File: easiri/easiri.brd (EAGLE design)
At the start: 50.8 x 50.8 mm, 44 parts

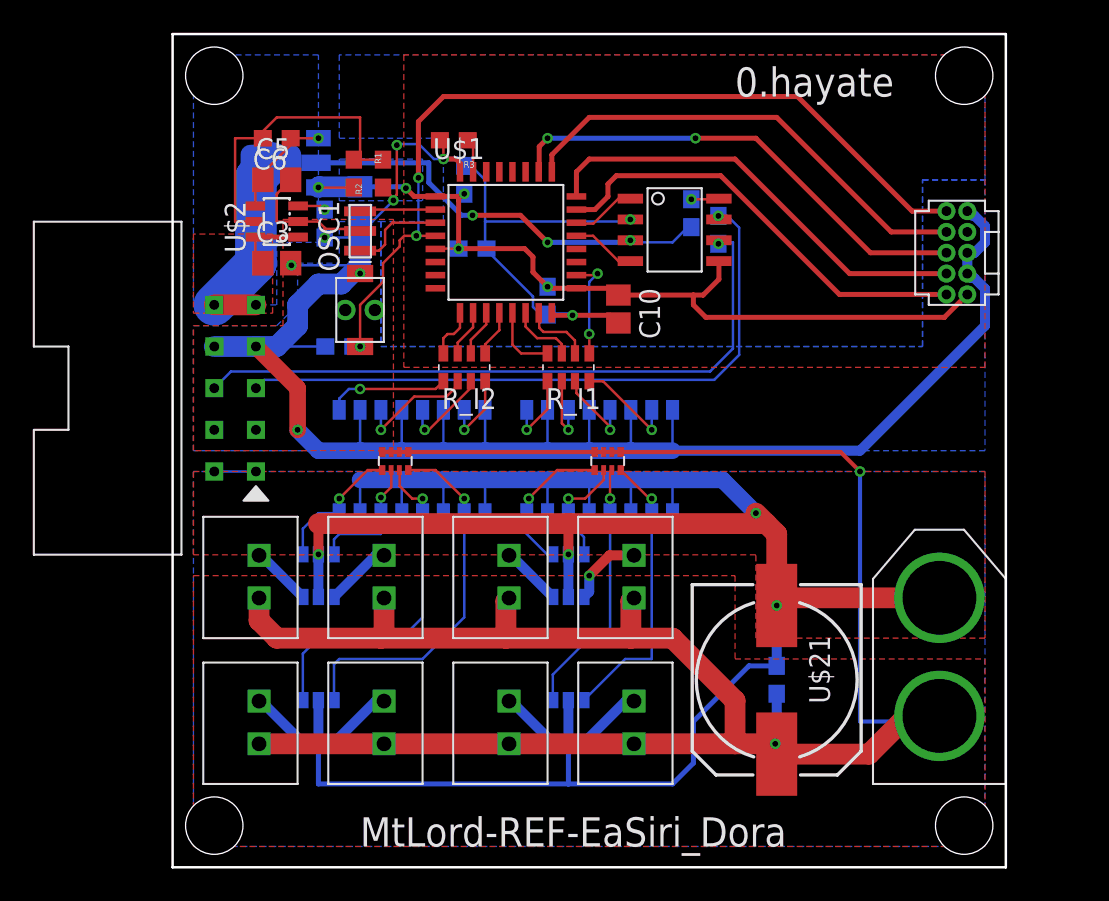
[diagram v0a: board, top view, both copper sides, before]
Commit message: usartとかを追加
電源確認or通信確認ようledをついか、pcでシリアルモニタによるデバッグができるようにusartを追加
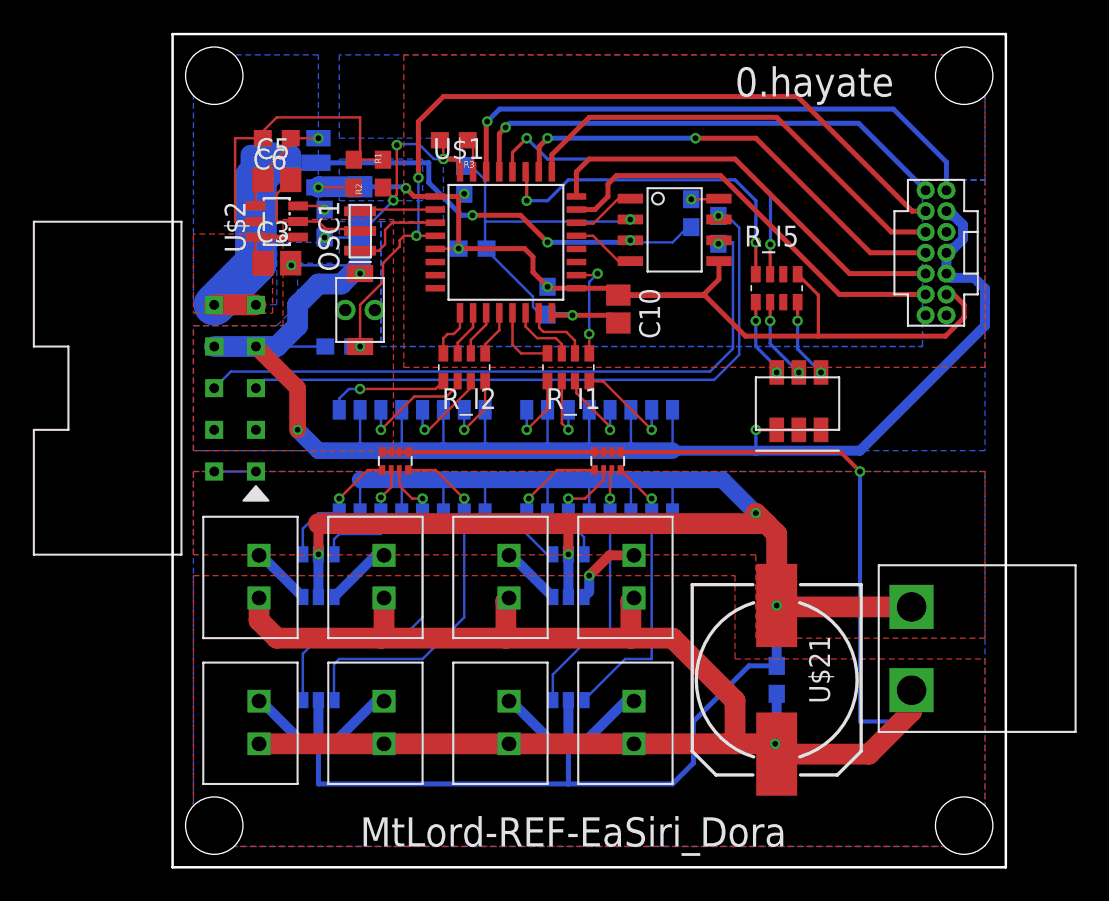
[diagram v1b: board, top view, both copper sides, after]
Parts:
- removed BOX10P-L1: BOX10P, user_conector:CON_HEDA10P_1.27
- added R_I5: 1k, user_rcl:0603X4RESISTOR
- added U$22: BOX14P, user_conector:CON_HEDA14P_1.27
- added U$23: RGB_LED, user_leds:RGB_LED
- U$12: value XT60 -> YUROBLOCK2; device user_conector:XT60 -> user_conector:YUROBLOCK2
- moved U$12 8.37 mm to (43.1, 8.26), turned to 0 degrees
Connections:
- new net N$11: R_I5.8, U$1.27
- new net N$40: R_I5.7, U$1.28
- new net N$42: R_I5.4, U$23.B_A
- new net N$43: R_I5.1, U$23.R_A
- new net N$44: R_I5.2, U$23.G_A
- new net RX: U$1.30, U$22.13
- new net TX: U$1.29, U$22.14
- net GND: now also U$22.11, U$22.5, U$22.7, U$23.B_K, U$23.G_K, U$23.R_K; no longer BOX10P-L1.3, BOX10P-L1.5, BOX10P-L1.9
- net GNDA: now also U$12.P$1; no longer U$12.-
- net JTCK: now also U$22.6; no longer BOX10P-L1.4
- net JTDI: now also U$22.10; no longer BOX10P-L1.8
- net JTDO: now also U$22.8; no longer BOX10P-L1.6
- net JTMS: now also U$22.4; no longer BOX10P-L1.2
- net NRST: now also U$22.12; no longer BOX10P-L1.10
- net V3.3: now also R_I5.5, U$22.3; no longer BOX10P-L1.1
- net VDD: now also U$12.P$2; no longer U$12.+
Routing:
- net RX: track 0.00 -> 34.5 mm, vias 0 -> 1
- net TX: track 0.00 -> 30.3 mm, vias 0 -> 1
- net N$40: track 0.00 -> 23.6 mm, vias 0 -> 2
- net N$11: track 0.00 -> 21.3 mm, vias 0 -> 2
- net V3.3: track 53.8 -> 64.6 mm
- net GND: track 155.6 -> 161.9 mm, vias 9 -> 10
- net N$44: track 0.00 -> 5.01 mm, vias 0 -> 2
- net N$42: track 0.00 -> 4.88 mm, vias 0 -> 2
- net N$43: track 0.00 -> 4.81 mm, vias 0 -> 2
- net JTMS: track 26.9 -> 25.6 mm
- net JTDO: track 29.5 -> 28.2 mm
- net NRST: track 52.9 -> 51.7 mm
- net JTDI: track 28.9 -> 27.7 mm
- net JTCK: track 27.3 -> 26.0 mm
- net GNDA: track 140.1 -> 138.9 mm

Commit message: Add files via upload
電源確認or通信確認ようledをついか、pcでシリアルモニタによるデバッグができるようにusartを追加
canのピンボックスが半分の位置になかったがどうしてもいやだったので半分の位置に来るようにした
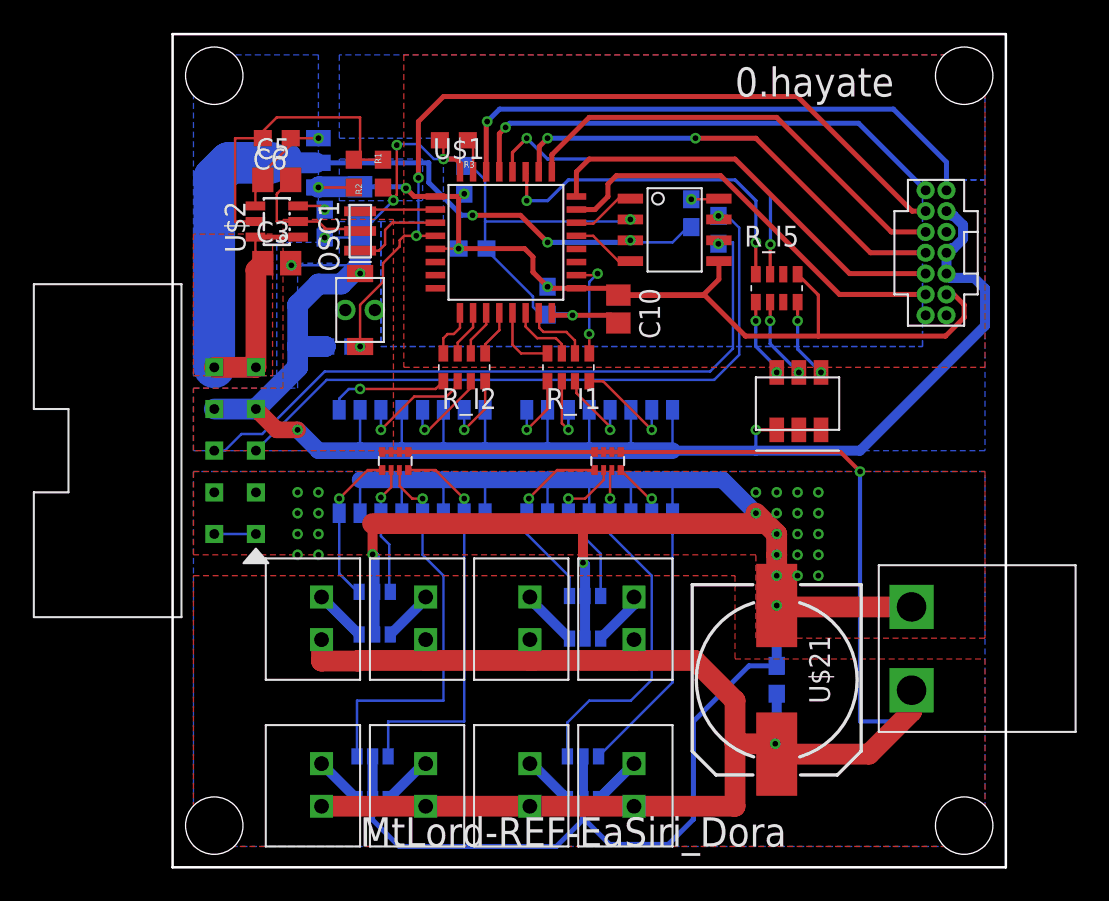
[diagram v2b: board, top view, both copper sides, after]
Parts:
- moved U$19 5.39 mm to (11.4, 1.27)
- moved U$11 4.76 mm to (12.2, 5.46)
- moved U$17 4.58 mm to (11.4, 11.4)
- moved U$20 4.58 mm to (17.8, 1.27)
- moved U$10 4.12 mm to (12.3, 15.5)
- moved U$15 4.02 mm to (24.1, 1.27)
- moved BOX10P-L2 3.81 mm to (2.54, 25.4)
- moved U$16 3.81 mm to (30.5, 1.27)
- moved U$18 3.59 mm to (17.8, 11.4)
- moved U$9 3.54 mm to (25.0, 5.46)
- moved U$13 2.84 mm to (24.1, 11.4)
- moved U$8 2.74 mm to (25.1, 15.2)
- moved U$14 2.54 mm to (30.5, 11.4)
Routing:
- net VCC: track 44.1 -> 58.1 mm
- net VDD: track 154.7 -> 146.2 mm
- net N$18: track 16.0 -> 22.2 mm
- net N$22: track 21.0 -> 24.2 mm
- net N$19: track 17.6 -> 20.7 mm
- net N$17: track 7.02 -> 9.98 mm
- net N$13: track 9.06 -> 11.8 mm
- net GNDA: track 138.9 -> 141.4 mm, vias 4 -> 28
- net N$23: track 22.7 -> 24.5 mm
- net CAN_L: track 40.3 -> 41.8 mm
- net CAN_H: track 39.9 -> 41.4 mm
- net N$26: track 4.68 -> 3.38 mm, vias 1 -> 0
- net N$20: track 8.40 -> 9.58 mm
- net N$27: track 4.10 -> 3.06 mm
- net N$29: track 4.10 -> 3.18 mm
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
